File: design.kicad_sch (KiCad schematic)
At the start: 80 parts, among them J1 2601-3108, J10 Conn_01x04, J11 Conn_01x04, J12 Conn_01x03, J13 Conn_01x03, J14 BM04B-SRSS-TB_LF__SN_, J2 2601-3108, J3 2601-3108, J4 TYPE-C-31-M-12, J5 SKEDD-UPDI-4, J6 Conn_01x04, J7 Conn_01x04, J8 Conn_01x04, J9 Conn_01x04, U1 ATtiny1616-S, U2 AP2112K-3.3, U3 CP2105

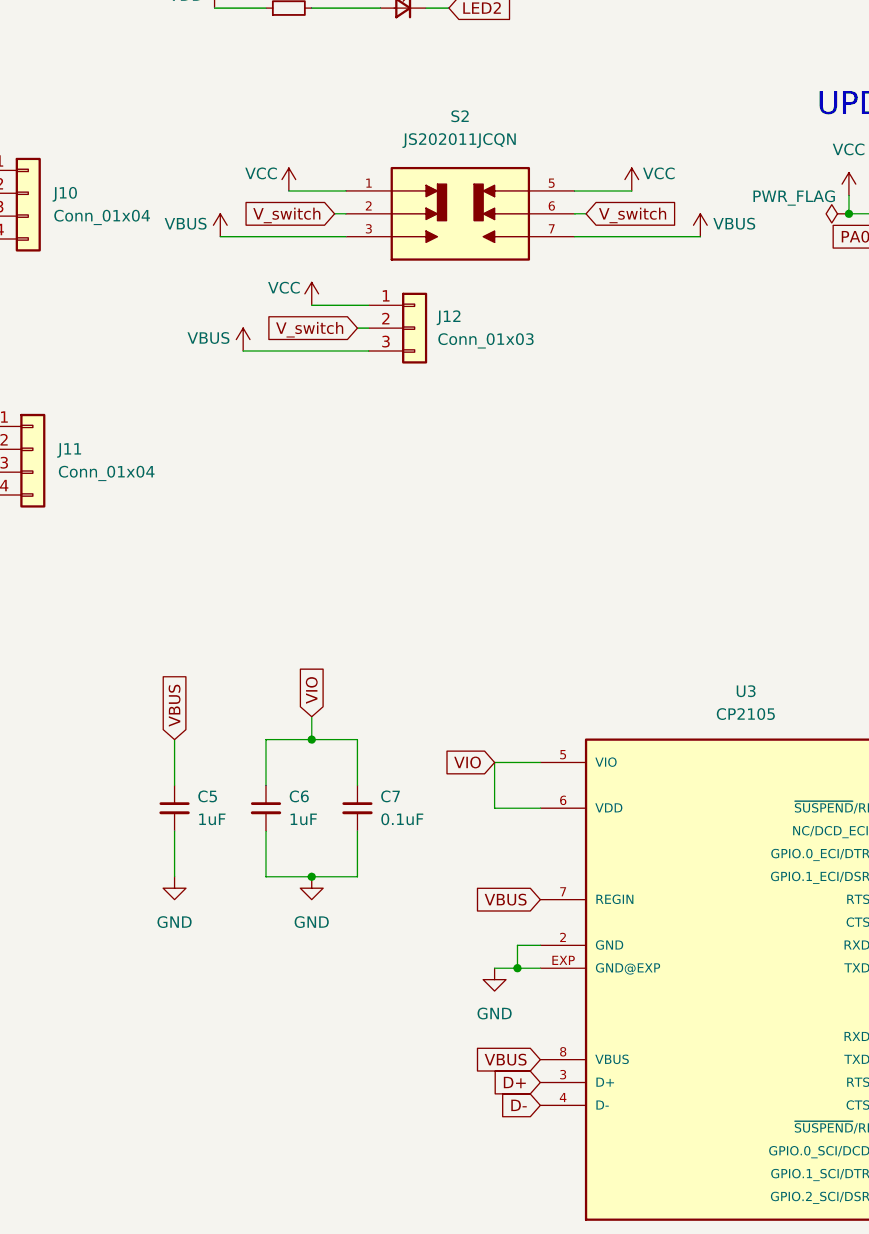
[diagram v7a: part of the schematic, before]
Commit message: use switchable power input for CP2105
closes #3
is not compatible with header pins only on J12
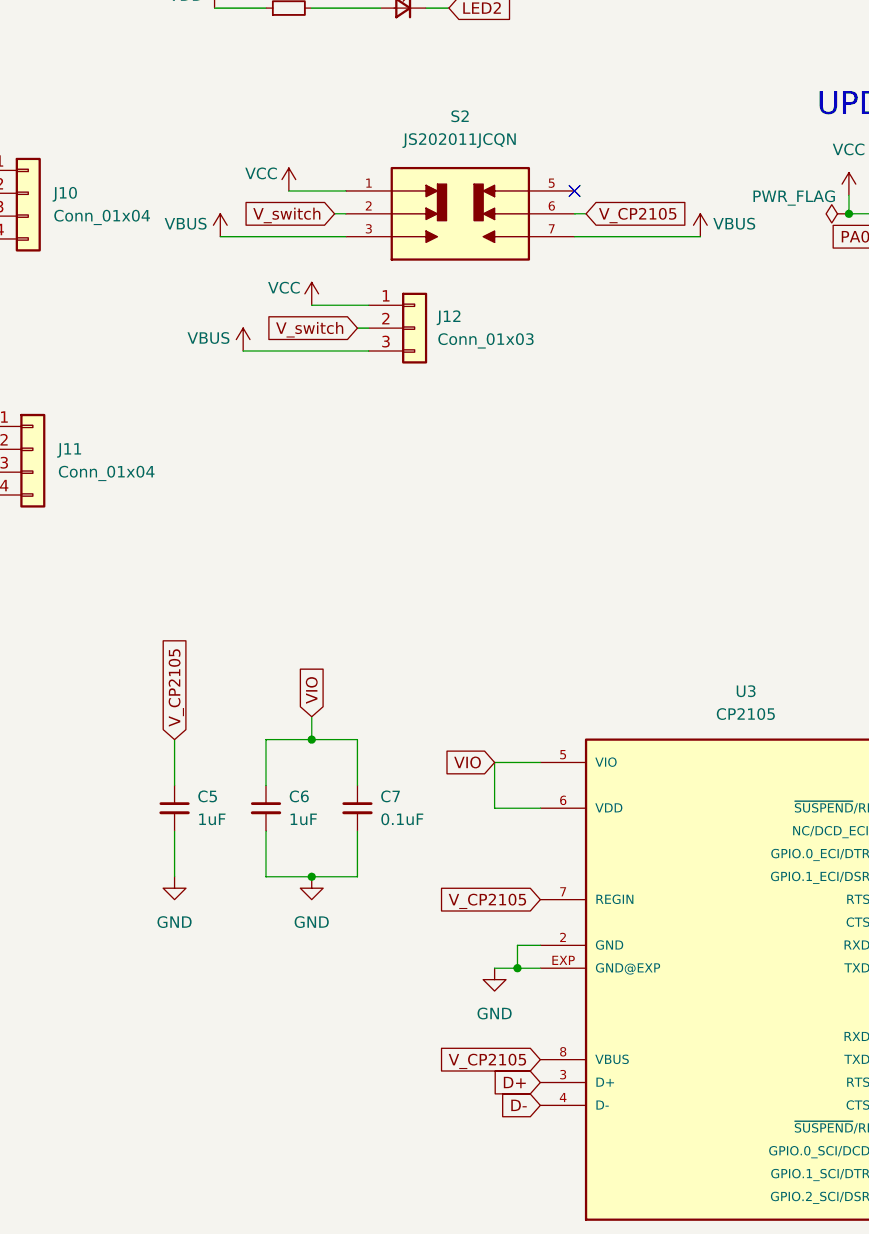
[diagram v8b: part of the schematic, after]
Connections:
- net VBUS: no longer C5.1, U3.7 (REGIN), U3.8 (VBUS)
- net VCC: no longer S2.5
- net V_switch: no longer S2.6
- new net V_CP2105: C5.1, S2.6, U3.7 (REGIN), U3.8 (VBUS)
- no-connect marks 13 -> 14
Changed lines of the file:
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@@
   (no_connect (at 248.92 233.68))
   (no_connect (at 68.58 45.72))
+  (no_connect (at 207.01 152.4))
   (no_connect (at 248.92 226.06))
   (no_connect (at 248.92 256.54))
@@
     (stroke (width 0) (type default) (color 0 0 0 0))
   )
-  (wire (pts (xy 207.01 152.4) (xy 213.36 152.4))
-    (stroke (width 0) (type default) (color 0 0 0 0))
-  )
   (wire (pts (xy 200.66 236.22) (xy 200.66 238.76))
     (stroke (width 0) (type default) (color 0 0 0 0))
@@
     )
   )
+  (global_label "V_CP2105" (shape input) (at 162.56 213.36 90) (fields_autoplaced)
+    (effects (font (size 1.27 1.27)) (justify left))
+    (property "Referenzen zwischen Schaltplänen" "${INTERSHEET_REFS}" (id 0) (at 162.4806 201.6015 90)
+      (effects (font (size 1.27 1.27)) (justify left) hide)
+    )
+  )
   (global_label "PB2" (shape input) (at 96.52 155.829 180) (fields_autoplaced)
     (effects (font (size 1.27 1.27)) (justify right))
@@
     )
   )
-  (global_label "VBUS" (shape input) (at 203.2 231.14 180) (fields_autoplaced)
+  (global_label "V_CP2105" (shape input) (at 203.2 231.14 180) (fields_autoplaced)
     (effects (font (size 1.27 1.27)) (justify right))
-    (property "Referenzen zwischen Schaltplänen" "${INTERSHEET_REFS}" (id 0) (at 195.9772 231.0606 0)
+    (property "Referenzen zwischen Schaltplänen" "${INTERSHEET_REFS}" (id 0) (at 191.4415 231.2194 0)
       (effects (font (size 1.27 1.27)) (justify right) hide)
     )
@@
     )
   )
-  (global_label "VBUS" (shape input) (at 203.2 248.92 180) (fields_autoplaced)
-    (effects (font (size 1.27 1.27)) (justify right))
-    (property "Referenzen zwischen Schaltplänen" "${INTERSHEET_REFS}" (id 0) (at 195.9772 248.8406 0)
-      (effects (font (size 1.27 1.27)) (justify right) hide)
-    )
-  )
   (global_label "PA0" (shape input) (at 91.44 78.74 0) (fields_autoplaced)
     (effects (font (size 1.27 1.27)) (justify left))
@@
     )
   )
-  (global_label "VBUS" (shape input) (at 162.56 213.36 90) (fields_autoplaced)
-    (effects (font (size 1.27 1.27)) (justify left))
-    (property "Referenzen zwischen Schaltplänen" "${INTERSHEET_REFS}" (id 0) (at 162.6394 206.1372 90)
-      (effects (font (size 1.27 1.27)) (justify left) hide)
-    )
-  )
   (global_label "PA5" (shape input) (at 24.257 160.02 180) (fields_autoplaced)
     (effects (font (size 1.27 1.27)) (justify right))
@@
     )
   )
-  (global_label "V_switch" (shape input) (at 208.28 154.94 0) (fields_autoplaced)
+  (global_label "V_CP2105" (shape input) (at 208.28 154.94 0) (fields_autoplaced)
     (effects (font (size 1.27 1.27)) (justify left))
-    (property "Referenzen zwischen Schaltplänen" "${INTERSHEET_REFS}" (id 0) (at 218.5871 154.8606 0)
+    (property "Referenzen zwischen Schaltplänen" "${INTERSHEET_REFS}" (id 0) (at 220.0385 154.8606 0)
       (effects (font (size 1.27 1.27)) (justify left) hide)
     )
@@
     )
   )
+  (global_label "V_CP2105" (shape input) (at 203.2 248.92 180) (fields_autoplaced)
+    (effects (font (size 1.27 1.27)) (justify right))
+    (property "Referenzen zwischen Schaltplänen" "${INTERSHEET_REFS}" (id 0) (at 191.4415 248.9994 0)
+      (effects (font (size 1.27 1.27)) (justify right) hide)
+    )
+  )
   (global_label "VIO" (shape input) (at 274.32 236.22 90) (fields_autoplaced)
     (effects (font (size 1.27 1.27)) (justify left))
@@
     (pin "1")
   )
-  (symbol (lib_id "power:VCC") (at 213.36 152.4 0) (mirror y) (unit 1)
-    (in_bom yes) (on_board yes)
-    (property "Reference" "#PWR0106" (id 0) (at 213.36 156.21 0)
-      (effects (font (size 1.27 1.27)) hide)
-    )
-    (property "Value" "VCC" (id 1) (at 216.408 150.495 0))
-    (property "Footprint" "" (id 2) (at 213.36 152.4 0)
-      (effects (font (size 1.27 1.27)) hide)
-    )
-    (property "Datasheet" "" (id 3) (at 213.36 152.4 0)
-      (effects (font (size 1.27 1.27)) hide)
-    )
-    (pin "1")
-  )
   (symbol (lib_id "power:GND") (at 388.62 190.5 0) (unit 1)
     (in_bom yes) (on_board yes) (fields_autoplaced)
@@
       (reference "#PWR0105") (unit 1) (value "VCC") (footprint "")
     )
-    (path "/4bea76cb-cb27-40bd-af2b-3b4521ea2235"
-      (reference "#PWR0106") (unit 1) (value "VCC") (footprint "")
-    )
     (path "/c097fc70-84bb-4a84-8a27-d6457ac14a2c"
